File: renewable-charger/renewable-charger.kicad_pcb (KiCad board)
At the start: 2 copper layers, 148.2 x 34.5 mm, 41 parts, among them J1 Solar Input, J2 USB_B_Micro, J3 Wind Output, J4 Battery, J5 Output, M1 Stepper_Motor_bipolar, Q1 P-channel 30V 4A MOSfet, Q2 P-channel 30V 4A MOSfet, U1 CN3791

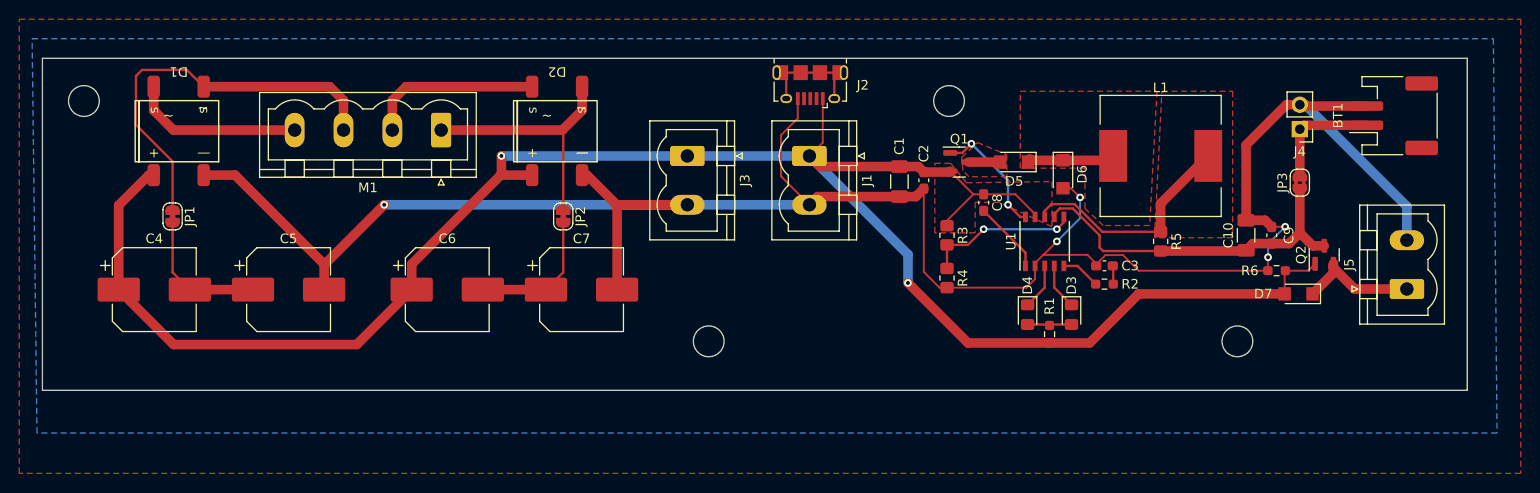
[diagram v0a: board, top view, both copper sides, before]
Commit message: Silkscreen additions for labelling, revision number, etc. added.  Final part of #4
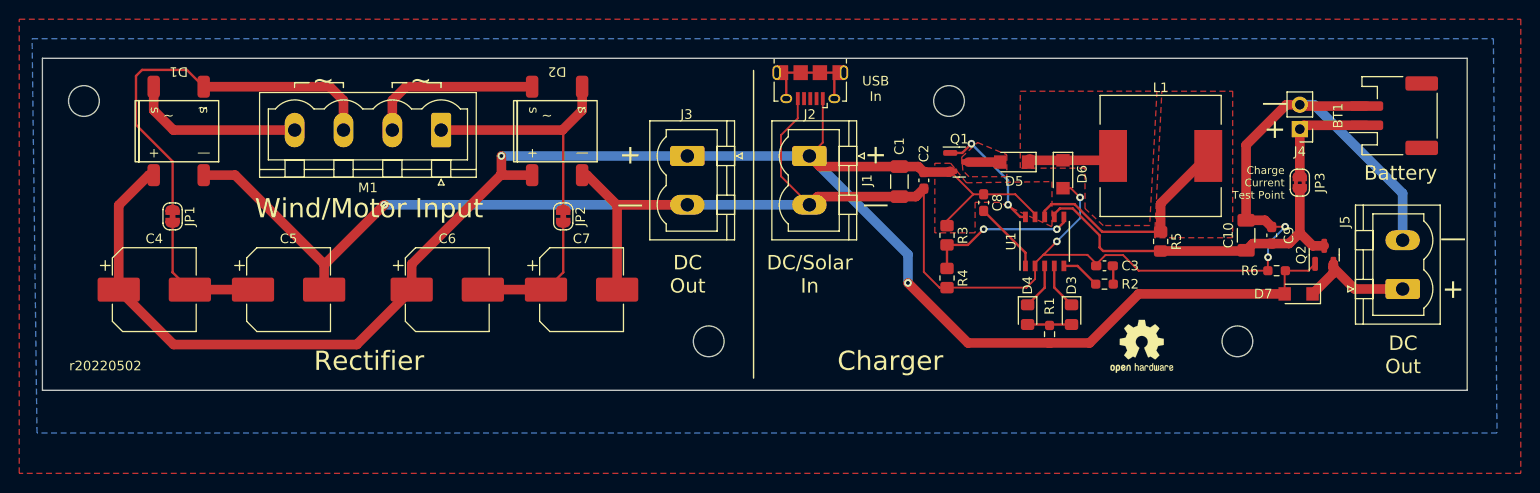
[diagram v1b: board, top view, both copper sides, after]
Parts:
- added REF**: OSHW-Logo2_7.3x6mm_SilkScreen, Symbol:OSHW-Logo2_7.3x6mm_SilkScreen, F.Cu at (188.1, 101.6)
- added REF**: WEEE-Logo_4.2x6mm_SilkScreen, Symbol:WEEE-Logo_4.2x6mm_SilkScreen, B.Cu at (197.7, 84.8)
- added REF**: OSHW-Logo2_7.3x6mm_SilkScreen, Symbol:OSHW-Logo2_7.3x6mm_SilkScreen, B.Cu at (87.6, 77.6)
- added REF**: RoHS-Logo_6mm_SilkScreen, Symbol:RoHS-Logo_6mm_SilkScreen, B.Cu at (189.6, 77.6)
- moved J5 0.44 mm to (215.2, 95.6)
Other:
- board text added: "+"
- board text added: "Battery"
- board text added: "Charge Current Test Point"
- board text added: "Charger"
- board text added: "DC Out"
- board text added: "DC/Solar In"
- board text added: "Rectifier"
- board text added: "USB In"
- board text added: "Wind/Motor Input"
- board text added: "r20220502"
- board text added: "tactile-electronics.tumblr.com mcqn.com/ibal233 github.com/Tactile-electronics/windmill-electronics"
- board text added: "~"
- board text added: "—"
